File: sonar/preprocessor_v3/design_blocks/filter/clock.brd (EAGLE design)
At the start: 34 x 20.3 mm, 16 parts

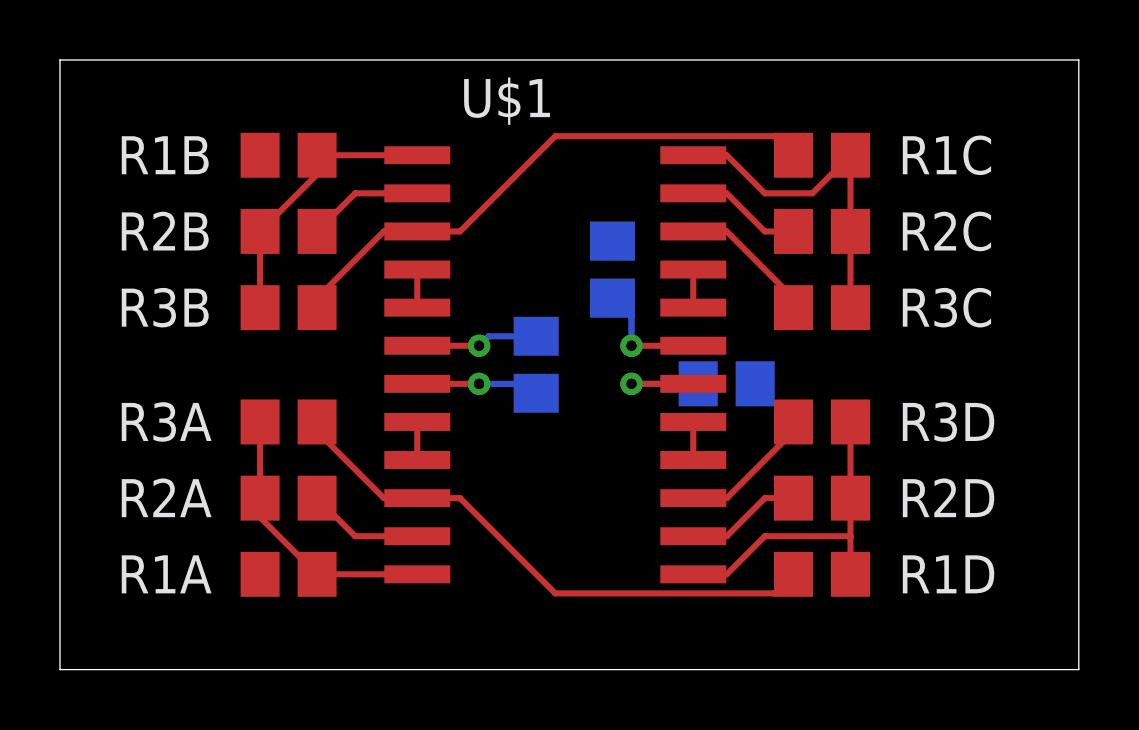
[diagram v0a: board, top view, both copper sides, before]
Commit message: updated filter design block, added clock design block
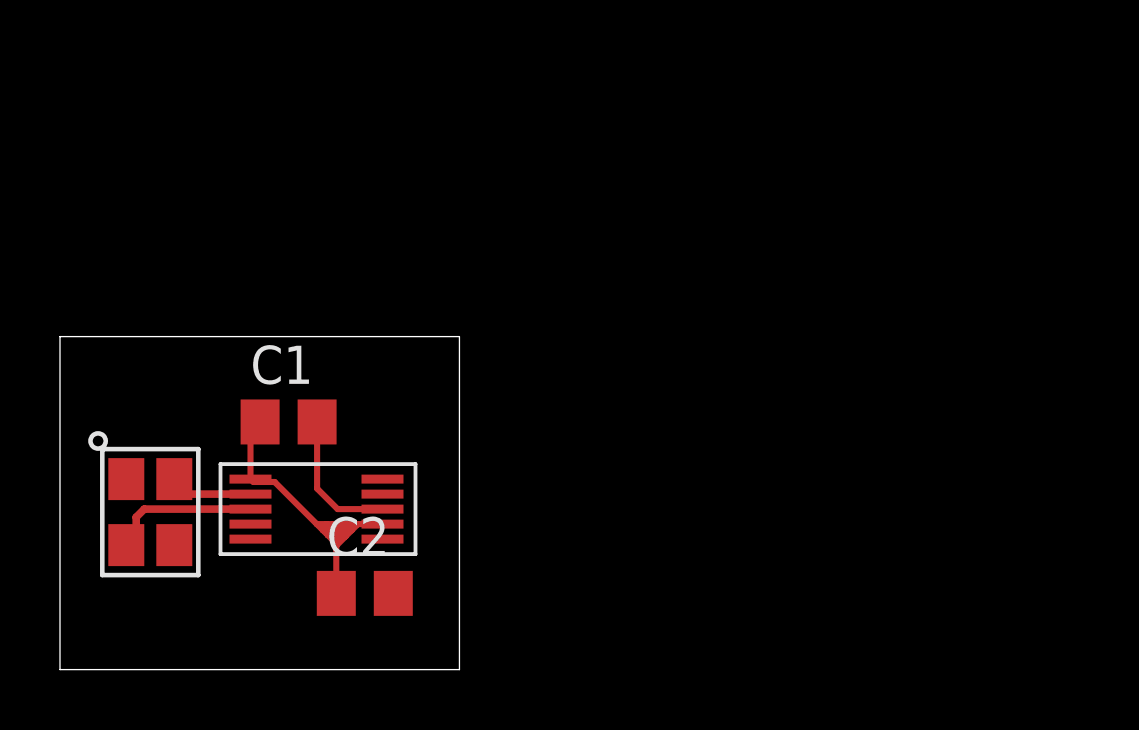
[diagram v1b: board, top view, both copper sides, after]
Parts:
- removed R1A, R1B, R1C, R1D, R3A, R3B, R3C, R3D: 350k, rcl:R0805
- removed R2A, R2B, R2C, R2D: 10k, rcl:R0805
- removed RCLK: 200, rcl:R0805
- removed U$1: LTC1264SMD, ARVP:SO24W
- added 25MHZ: FA-238, ARVP:FA-238
- added U$2: SI5351A, ARVP:MSOP-10
- C1, C2: value 0.1u -> 0.47u
- moved C2 13.6 mm to (10.2, 2.54), flipped to the top, turned to 0 degrees
- moved C1 8.47 mm to (7.62, 8.26), flipped to the top, turned to 0 degrees
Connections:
- removed net +5V: C1.1, U$1.7
- removed net -5V: C2.2, U$1.19
- removed net CLK: RCLK.2
- removed net IN_A: R1A.1
- removed net IN_B: R1B.1
- removed net N$10: R1B.2, R2B.1, R3B.1, U$1.1
- removed net N$12: U$1.4, U$1.5
- removed net N$13: U$1.20, U$1.21
- removed net N$14: RCLK.1, U$1.18
- removed net N$16: R2A.2, U$1.11
- removed net N$18: U$1.8, U$1.9
- removed net N$2: R2D.2, U$1.14
- removed net N$3: R1D.2, R2D.1, R3D.1, U$1.13
- removed net N$32: R1A.2, R2A.1, R3A.1, U$1.12
- removed net N$5: U$1.16, U$1.17
- removed net N$6: R2C.1, U$1.23
- removed net N$7: R1C.1, R2C.2, R3C.2, U$1.24
- removed net N$9: R2B.2, U$1.2
- removed net OUT_2ND_A: R1D.1, R3A.2, U$1.10
- removed net OUT_2ND_ORDER_B: R1C.2, R3B.2, U$1.3
- removed net OUT_A: R3D.2, U$1.15
- removed net OUT_B: R3C.1, U$1.22
- new net CLK0: U$2.P$10
- new net CLK1: U$2.P$9
- new net CLK2: U$2.P$6
- new net N$27: 25MHZ.P$4, U$2.P$2
- new net N$28: 25MHZ.P$2, U$2.P$3
- new net SCL: U$2.P$4
- new net SDA: U$2.P$5
- new net VDD: C1.1, C2.1, U$2.P$1, U$2.P$7
- net GND: now also C2.2, U$2.P$8; no longer C2.1, U$1.6
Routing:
- net OUT_2ND_ORDER_B: track 18.7 -> 0.00 mm
- net OUT_2ND_A: track 18.7 -> 0.00 mm
- net VDD: track 0.00 -> 14.3 mm
- net N$7: track 11.3 -> 0.00 mm
- net N$3: track 10.8 -> 0.00 mm
- net N$32: track 9.21 -> 0.00 mm
- net N$10: track 9.21 -> 0.00 mm
- net N$28: track 0.00 -> 4.99 mm
- net OUT_B: track 4.58 -> 0.00 mm
- net OUT_A: track 4.58 -> 0.00 mm
- net N$14: track 4.28 -> 0.00 mm, vias 1 -> 0
- net +5V: track 4.10 -> 0.00 mm, vias 1 -> 0
- net -5V: track 3.91 -> 0.00 mm, vias 1 -> 0
- net N$9: track 3.87 -> 0.00 mm
- net N$6: track 3.87 -> 0.00 mm
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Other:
- board size 34 x 20.3 mm -> 13.3 x 11.1 mm
